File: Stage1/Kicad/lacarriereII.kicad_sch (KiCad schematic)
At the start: 87 parts, among them J1 USB_C_Receptacle_USB2.0, J2 Conn_02x06, J3 Conn_01x06_Pin, U1 PCA9557PW, U10 XC6206P282MR, U11 XC6206P132MR, U12 ESP32_WROVER, U14 BME280, U16 BME280, U2 USBLC6-2SC6, U3 BQ25171QWDRCRQ1, U4 CH340C, U5 SIM800L-CORE, U6 UMH3N, U7 FS8205, U8 HY2112, U9 TLV61070A

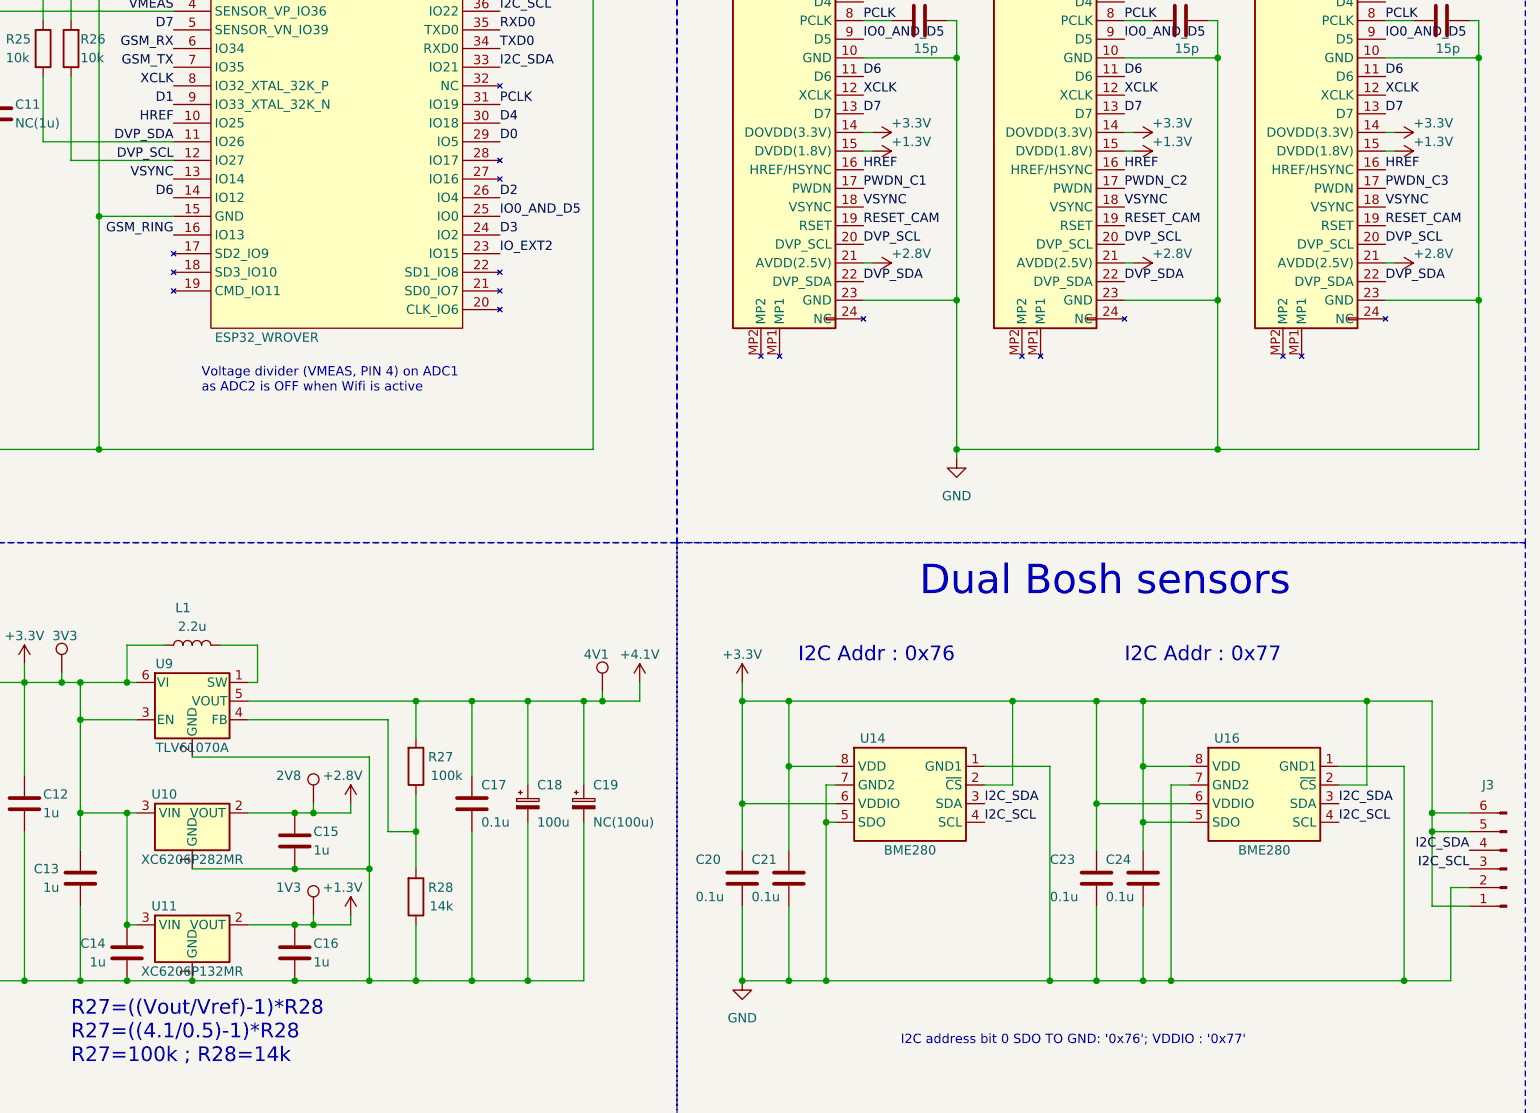
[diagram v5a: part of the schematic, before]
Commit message: [change] via size to be compatible witch jlc capabilities specs
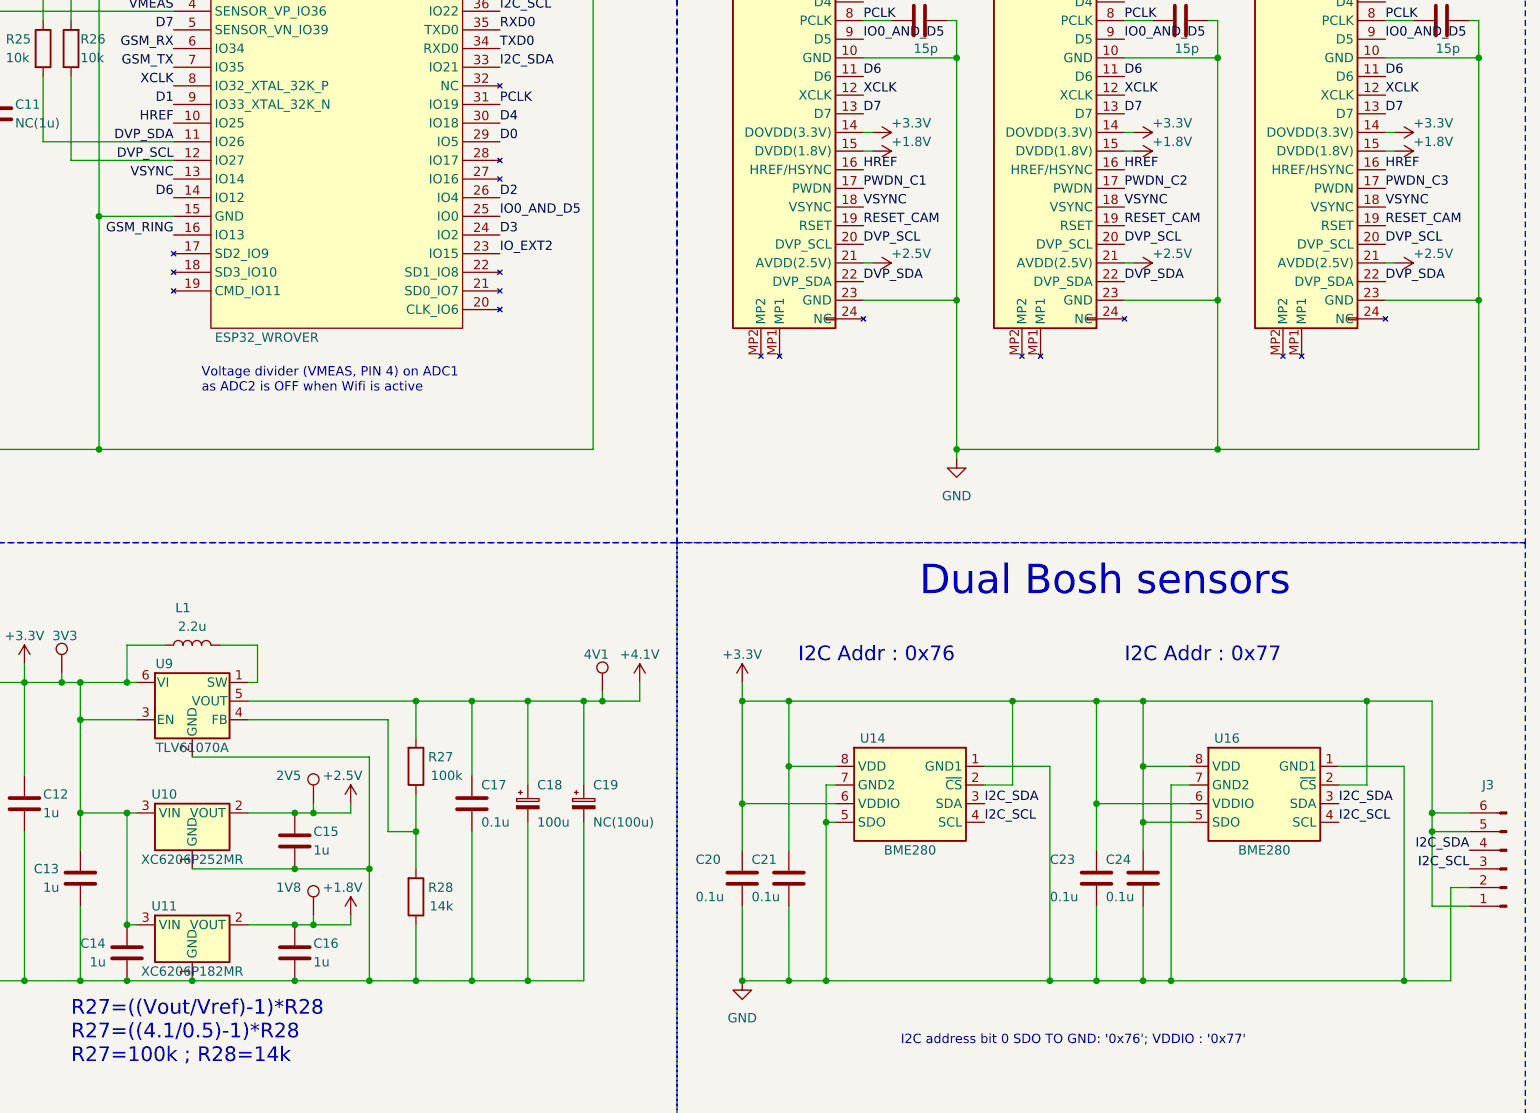
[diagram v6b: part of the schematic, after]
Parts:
- U10: value XC6206P282MR -> XC6206P252MR
- U11: value XC6206P132MR -> XC6206P182MR
- renumbered 1V3 to 1V8, 2V8 to 2V5
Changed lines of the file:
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@@
       (effects (font (size 1.27 1.27)) hide)
     )
-    (property "Value" "+2.8V" (at 318.77 88.9 90)
+    (property "Value" "+2.5V" (at 318.77 88.9 90)
       (effects (font (size 1.27 1.27)) (justify left))
     )
@@
       (effects (font (size 1.27 1.27)) hide)
     )
-    (property "Value" "+2.8V" (at 241.3 160.02 0)
+    (property "Value" "+2.5V" (at 241.3 160.02 0)
       (effects (font (size 1.27 1.27)) (justify left))
     )
@@
       (effects (font (size 1.27 1.27)) hide)
     )
-    (property "Value" "+2.8V" (at 354.33 88.9 90)
+    (property "Value" "+2.5V" (at 354.33 88.9 90)
       (effects (font (size 1.27 1.27)) (justify left))
     )
@@
       (effects (font (size 1.27 1.27)) hide)
     )
-    (property "Value" "+1.3V" (at 389.89 73.66 90)
+    (property "Value" "+1.8V" (at 389.89 73.66 90)
       (effects (font (size 1.27 1.27)) (justify left))
     )
@@
   (symbol (lib_id "Connector:TestPoint") (at 240.03 163.83 0) (unit 1)
     (in_bom yes) (on_board yes) (dnp no)
-    (property "Reference" "2V8" (at 234.95 160.02 0)
+    (property "Reference" "2V5" (at 234.95 160.02 0)
       (effects (font (size 1.27 1.27)) (justify left))
     )
@@
       (project "lacarriereII"
         (path "/3c8426f4-ef7d-418b-9048-6c57d75d81b5"
-          (reference "2V8") (unit 1)
+          (reference "2V5") (unit 1)
         )
       )
@@
       (effects (font (size 1.27 1.27)) hide)
     )
-    (property "Value" "+1.3V" (at 318.77 73.66 90)
+    (property "Value" "+1.8V" (at 318.77 73.66 90)
       (effects (font (size 1.27 1.27)) (justify left))
     )
@@
       (effects (font (size 1.27 1.27)))
     )
-    (property "Value" "XC6206P282MR" (at 223.52 171.45 0)
+    (property "Value" "XC6206P252MR" (at 223.52 171.45 0)
       (effects (font (size 1.27 1.27)))
     )
@@
       (effects (font (size 1.27 1.27)) hide)
     )
-    (property "Value" "+2.8V" (at 389.89 88.9 90)
+    (property "Value" "+2.5V" (at 389.89 88.9 90)
       (effects (font (size 1.27 1.27)) (justify left))
     )
@@
       (effects (font (size 1.27 1.27)) hide)
     )
-    (property "Value" "+1.3V" (at 241.3 175.26 0)
+    (property "Value" "+1.8V" (at 241.3 175.26 0)
       (effects (font (size 1.27 1.27)) (justify left))
     )
@@
       (effects (font (size 1.27 1.27)))
     )
-    (property "Value" "XC6206P132MR" (at 223.52 186.69 0)
+    (property "Value" "XC6206P182MR" (at 223.52 186.69 0)
       (effects (font (size 1.27 1.27)))
     )
@@
   (symbol (lib_id "Connector:TestPoint") (at 240.03 179.07 0) (unit 1)
     (in_bom yes) (on_board yes) (dnp no)
-    (property "Reference" "1V3" (at 234.95 175.26 0)
+    (property "Reference" "1V8" (at 234.95 175.26 0)
       (effects (font (size 1.27 1.27)) (justify left))
     )
@@
       (project "lacarriereII"
         (path "/3c8426f4-ef7d-418b-9048-6c57d75d81b5"
-          (reference "1V3") (unit 1)
+          (reference "1V8") (unit 1)
         )
       )
@@
       (effects (font (size 1.27 1.27)) hide)
     )
-    (property "Value" "+1.3V" (at 354.33 73.66 90)
-      (effects (font (size 1.27 1.27)) (justify left))
-    )
+    (property "Value" "+1.8V" (at 354.33 73.66 90)
+      (effects (font (size 1.27 1.27)) (justify left))
+    )
